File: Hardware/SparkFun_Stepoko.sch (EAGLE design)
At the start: 178 parts, among them J1 AVR ISP, Q1 16MHZ, Q2 100A/100V, U1 ATMEGA328, U10 +12v, U2 FT232RLSSOP, U3 74LVC1G04, U4 LM25011, U5 DRV8811, U6 74HC7014D, U7 7432SE, U8 DRV8811, U9 DRV8811

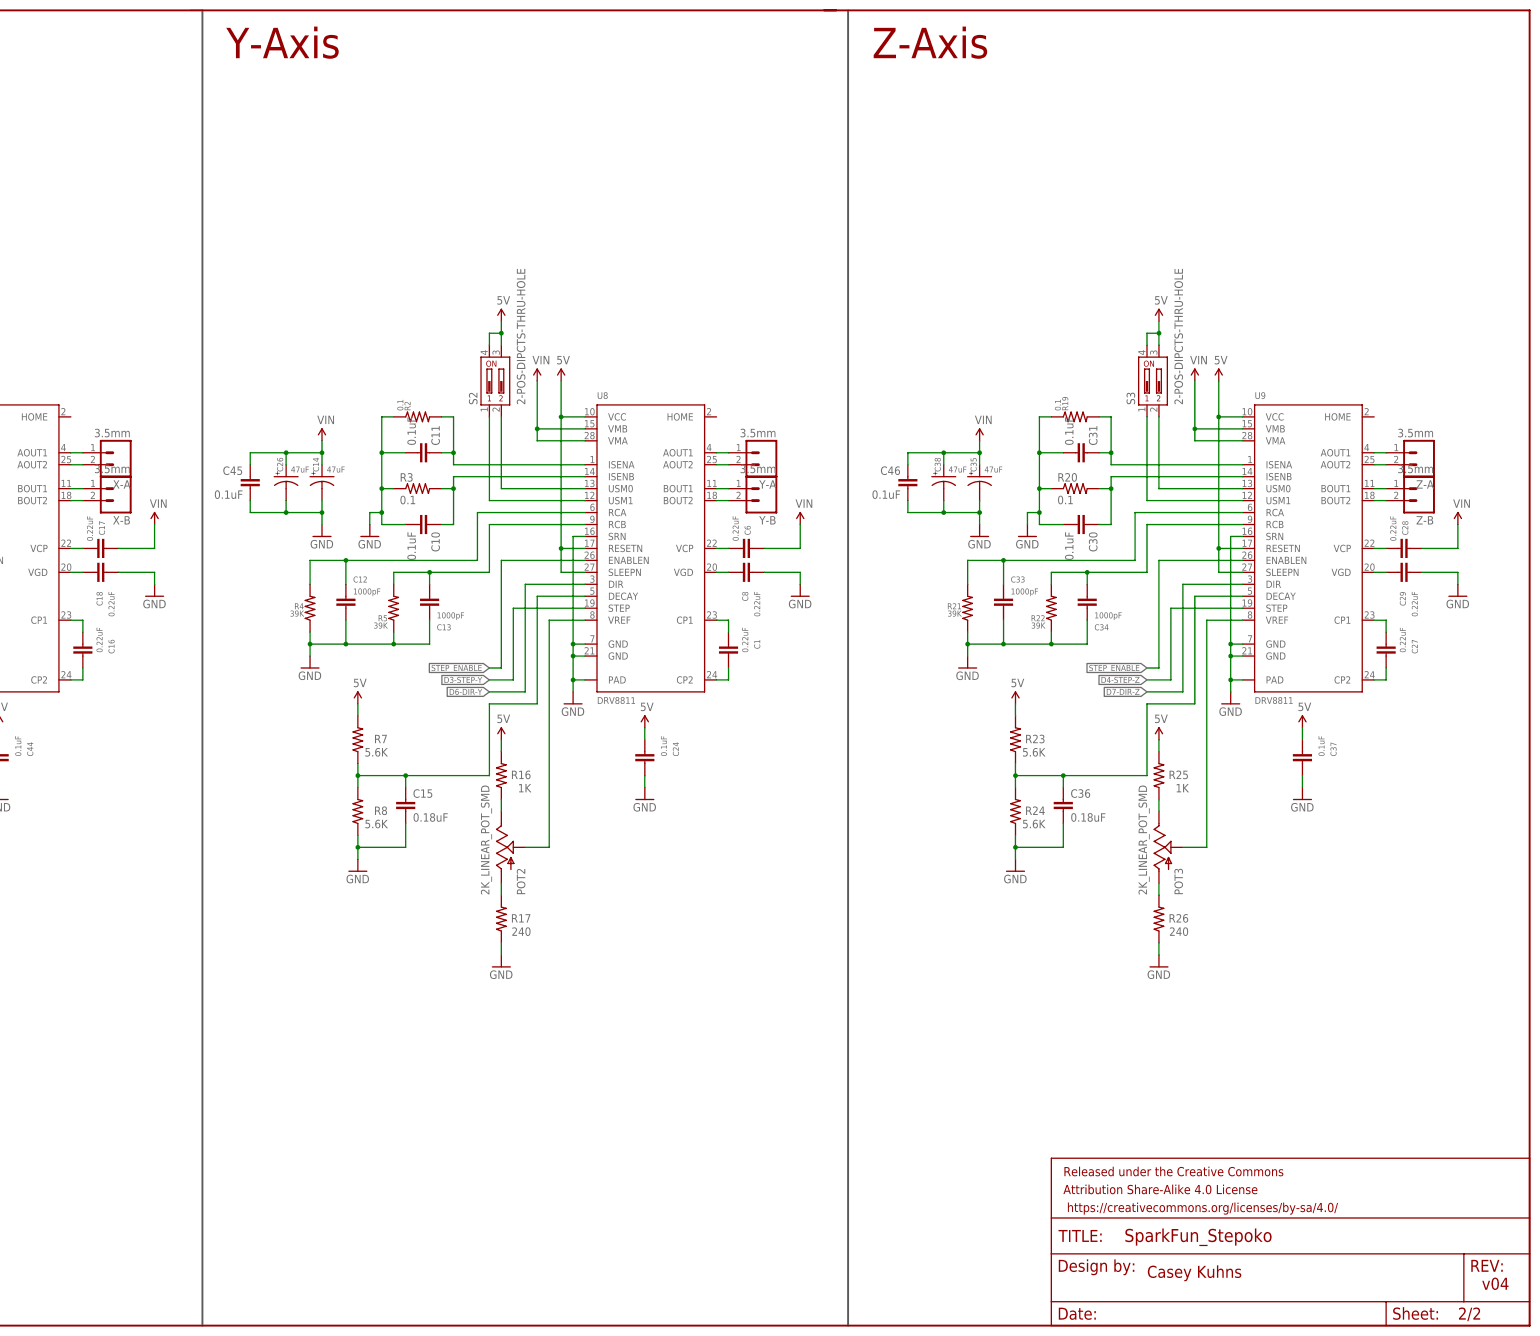
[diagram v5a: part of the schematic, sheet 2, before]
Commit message: corrected issued from Design review. Opened up holes to prevent potential shorts, schematic cleanup.
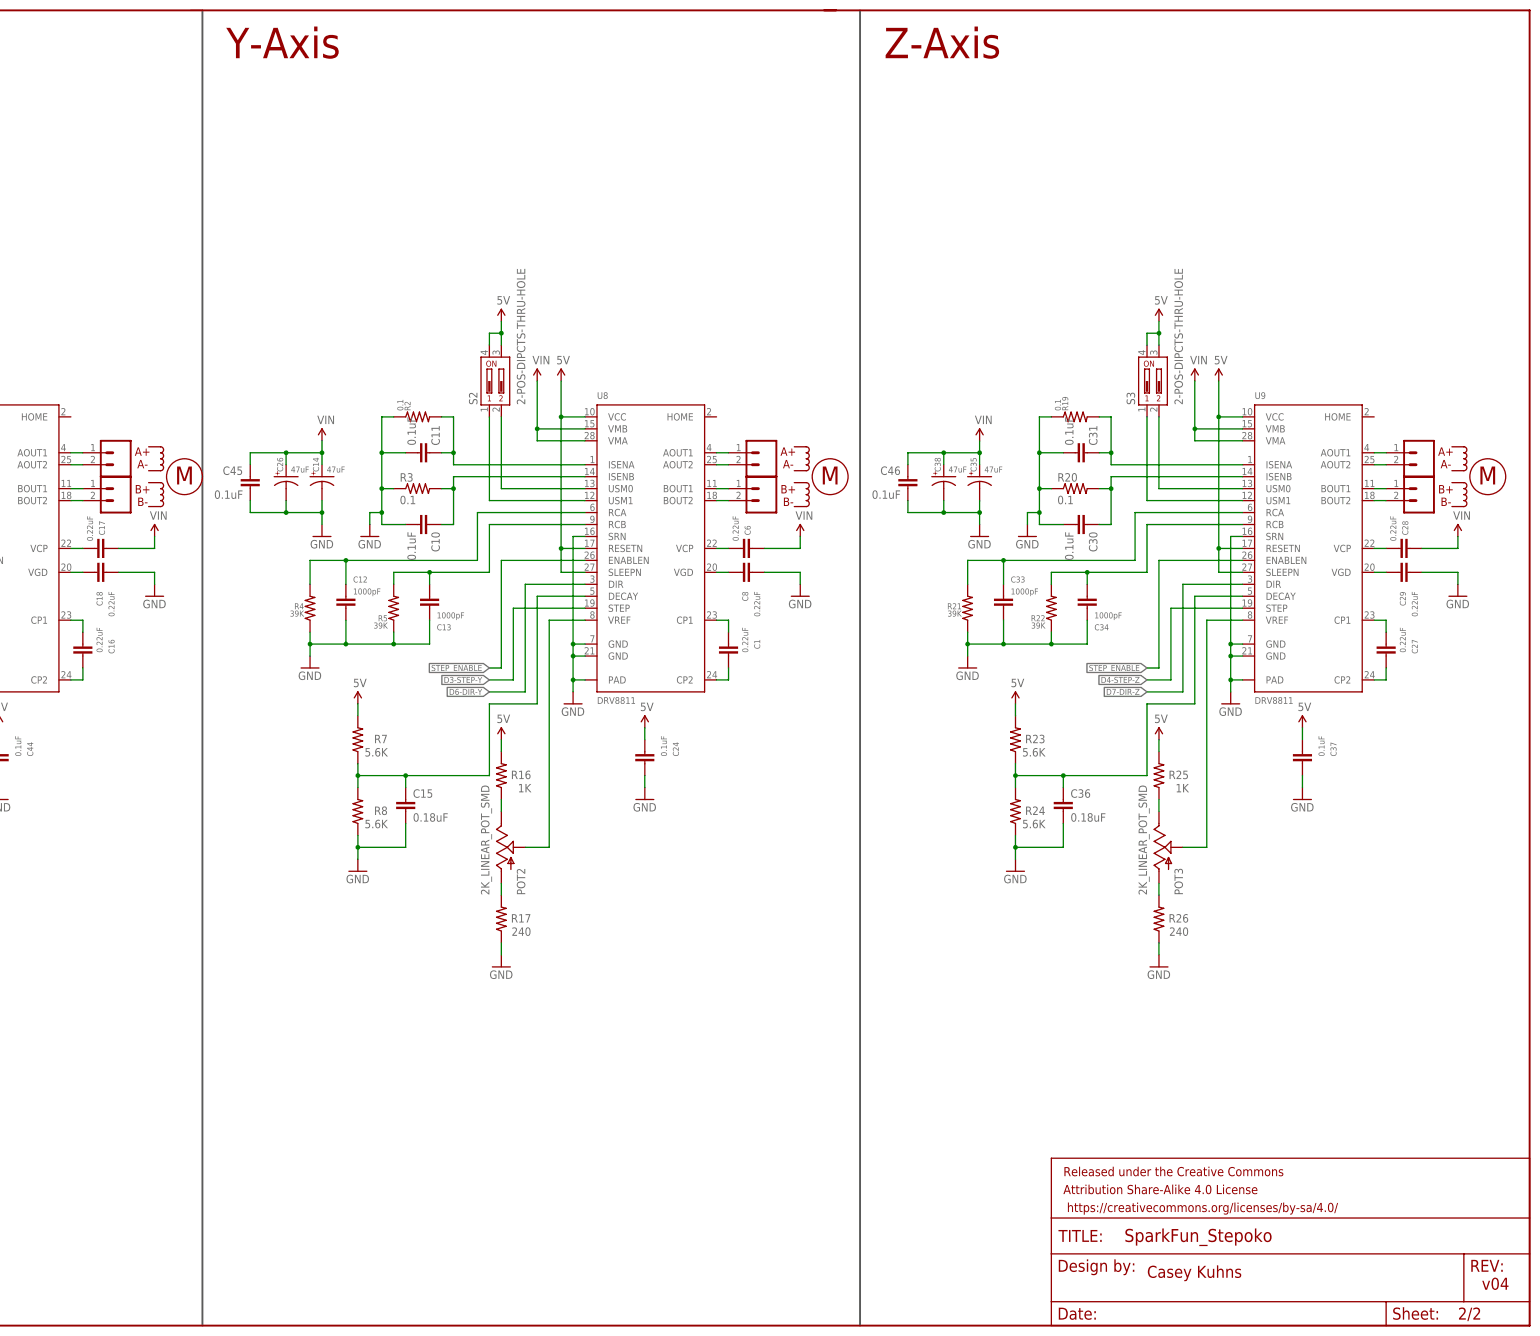
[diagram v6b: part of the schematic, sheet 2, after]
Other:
- note added: "A+ A- B+ B-"
- note added: "M"
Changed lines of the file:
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@@
 <setting verticaltext="up"/>
 </settings>
-<grid distance="0.1" unitdist="inch" unit="inch" style="lines" multiple="1" display="no" altdistance="0.01" altunitdist="inch" altunit="inch"/>
+<grid distance="0.1" unitdist="inch" unit="inch" style="lines" multiple="1" display="yes" altdistance="0.01" altunitdist="inch" altunit="inch"/>
 <layers>
 <layer number="1" name="Top" color="4" fill="1" visible="no" active="no"/>
@@
 <instance part="R52" gate="G$1" x="213.36" y="40.64" smashed="yes" rot="MR270">
 <attribute name="NAME" x="214.8586" y="36.83" size="1.778" layer="95" rot="MR90"/>
-<attribute name="VALUE" x="215.138" y="41.91" size="1.778" layer="96" rot="MR90"/>
+<attribute name="VALUE" x="210.058" y="36.83" size="1.778" layer="96" rot="MR90"/>
 </instance>
 <instance part="GND36" gate="1" x="213.36" y="30.48" rot="MR0"/>
@@
 <instance part="U10" gate="G$1" x="91.44" y="63.5" smashed="yes">
 <attribute name="NAME" x="86.36" y="55.88" size="1.778" layer="95"/>
-<attribute name="VALUE" x="86.36" y="73.66" size="1.778" layer="96"/>
+<attribute name="VALUE" x="86.36" y="53.34" size="1.778" layer="96"/>
 </instance>
 <instance part="GND60" gate="1" x="91.44" y="50.8" rot="MR0"/>
@@
 <text x="5.08" y="269.24" size="6.4516" layer="94" ratio="15">X-Axis</text>
 <text x="154.94" y="269.24" size="6.4516" layer="94" ratio="15">Y-Axis</text>
-<text x="292.1" y="269.24" size="6.4516" layer="94" ratio="15">Z-Axis</text>
+<text x="294.64" y="269.24" size="6.4516" layer="94" ratio="15">Z-Axis</text>
 <wire x1="147.32" y1="279.4" x2="149.86" y2="279.4" width="0.1524" layer="94"/>
 <wire x1="149.86" y1="279.4" x2="149.86" y2="0" width="0.4064" layer="97"/>
 <wire x1="284.48" y1="279.4" x2="281.94" y2="279.4" width="0.4064" layer="94"/>
-<wire x1="287.02" y1="279.4" x2="287.02" y2="0" width="0.4064" layer="97"/>
+<wire x1="289.56" y1="279.4" x2="289.56" y2="0" width="0.4064" layer="97"/>
 <text x="421.64" y="7.62" size="2.54" layer="94">v04</text>
 <text x="350.52" y="10.16" size="2.54" layer="94">Casey Kuhns</text>
+<wire x1="138.43" y1="181.61" x2="140.97" y2="181.61" width="0.1524" layer="94"/>
+<wire x1="138.43" y1="186.69" x2="140.97" y2="186.69" width="0.1524" layer="94"/>
+<wire x1="140.97" y1="186.69" x2="140.97" y2="185.42" width="0.1524" layer="94" curve="-180"/>
+<wire x1="140.97" y1="185.42" x2="140.97" y2="184.15" width="0.1524" layer="94" curve="-180"/>
+<wire x1="140.97" y1="184.15" x2="140.97" y2="182.88" width="0.1524" layer="94" curve="-180"/>
+<wire x1="140.97" y1="182.88" x2="140.97" y2="181.61" width="0.1524" layer="94" curve="-180"/>
+<wire x1="138.43" y1="173.99" x2="140.97" y2="173.99" width="0.1524" layer="94"/>
+<wire x1="138.43" y1="179.07" x2="140.97" y2="179.07" width="0.1524" layer="94"/>
+<wire x1="140.97" y1="179.07" x2="140.97" y2="177.8" width="0.1524" layer="94" curve="-180"/>
+<wire x1="140.97" y1="177.8" x2="140.97" y2="176.53" width="0.1524" layer="94" curve="-180"/>
+<wire x1="140.97" y1="176.53" x2="140.97" y2="175.26" width="0.1524" layer="94" curve="-180"/>
+<wire x1="140.97" y1="175.26" x2="140.97" y2="173.99" width="0.1524" layer="94" curve="-180"/>
+<circle x="146.05" y="180.34" radius="3.81" width="0.1524" layer="94"/>
+<text x="146.05" y="180.594" size="3.81" layer="94" font="fixed" ratio="14" align="center">M</text>
+<wire x1="275.59" y1="181.61" x2="278.13" y2="181.61" width="0.1524" layer="94"/>
+<wire x1="275.59" y1="186.69" x2="278.13" y2="186.69" width="0.1524" layer="94"/>
+<wire x1="278.13" y1="186.69" x2="278.13" y2="185.42" width="0.1524" layer="94" curve="-180"/>
+<wire x1="278.13" y1="185.42" x2="278.13" y2="184.15" width="0.1524" layer="94" curve="-180"/>
+<wire x1="278.13" y1="184.15" x2="278.13" y2="182.88" width="0.1524" layer="94" curve="-180"/>
+<wire x1="278.13" y1="182.88" x2="278.13" y2="181.61" width="0.1524" layer="94" curve="-180"/>
+<wire x1="275.59" y1="173.99" x2="278.13" y2="173.99" width="0.1524" layer="94"/>
+<wire x1="275.59" y1="179.07" x2="278.13" y2="179.07" width="0.1524" layer="94"/>
+<wire x1="278.13" y1="179.07" x2="278.13" y2="177.8" width="0.1524" layer="94" curve="-180"/>
+<wire x1="278.13" y1="177.8" x2="278.13" y2="176.53" width="0.1524" layer="94" curve="-180"/>
+<wire x1="278.13" y1="176.53" x2="278.13" y2="175.26" width="0.1524" layer="94" curve="-180"/>
+<wire x1="278.13" y1="175.26" x2="278.13" y2="173.99" width="0.1524" layer="94" curve="-180"/>
+<circle x="283.21" y="180.34" radius="3.81" width="0.1524" layer="94"/>
+<text x="283.21" y="180.594" size="3.81" layer="94" font="fixed" ratio="14" align="center">M</text>
+<wire x1="415.29" y1="181.61" x2="417.83" y2="181.61" width="0.1524" layer="94"/>
+<wire x1="415.29" y1="186.69" x2="417.83" y2="186.69" width="0.1524" layer="94"/>
+<wire x1="417.83" y1="186.69" x2="417.83" y2="185.42" width="0.1524" layer="94" curve="-180"/>
+<wire x1="417.83" y1="185.42" x2="417.83" y2="184.15" width="0.1524" layer="94" curve="-180"/>
+<wire x1="417.83" y1="184.15" x2="417.83" y2="182.88" width="0.1524" layer="94" curve="-180"/>
+<wire x1="417.83" y1="182.88" x2="417.83" y2="181.61" width="0.1524" layer="94" curve="-180"/>
+<wire x1="415.29" y1="173.99" x2="417.83" y2="173.99" width="0.1524" layer="94"/>
+<wire x1="415.29" y1="179.07" x2="417.83" y2="179.07" width="0.1524" layer="94"/>
+<wire x1="417.83" y1="179.07" x2="417.83" y2="177.8" width="0.1524" layer="94" curve="-180"/>
+<wire x1="417.83" y1="177.8" x2="417.83" y2="176.53" width="0.1524" layer="94" curve="-180"/>
+<wire x1="417.83" y1="176.53" x2="417.83" y2="175.26" width="0.1524" layer="94" curve="-180"/>
+<wire x1="417.83" y1="175.26" x2="417.83" y2="173.99" width="0.1524" layer="94" curve="-180"/>
+<circle x="422.91" y="180.34" radius="3.81" width="0.1524" layer="94"/>
+<text x="422.91" y="180.594" size="3.81" layer="94" font="fixed" ratio="14" align="center">M</text>
+<text x="137.16" y="180.34" size="1.778" layer="94" ratio="14" align="center">A+
+A-
+B+
+B-</text>
+<text x="274.32" y="180.34" size="1.778" layer="94" ratio="14" align="center">A+
+A-
+B+
+B-</text>
+<text x="414.02" y="180.34" size="1.778" layer="94" ratio="14" align="center">A+
+A-
+B+
+B-</text>
 </plain>
 <instances>
@@
 <instance part="GND29" gate="1" x="106.68" y="111.76"/>
 <instance part="SUPPLY3" gate="G$1" x="83.82" y="200.66"/>
-<instance part="SUPPLY5" gate="G$1" x="139.7" y="170.18"/>
+<instance part="SUPPLY5" gate="G$1" x="139.7" y="167.64"/>
 <instance part="POT1" gate="G$1" x="76.2" y="101.6"/>
 <instance part="R1" gate="G$1" x="76.2" y="86.36" smashed="yes" rot="R90">
@@
 <attribute name="VALUE" x="82.55" y="84.582" size="1.778" layer="96" rot="R180"/>
 </instance>
-<instance part="X-A" gate="G$1" x="132.08" y="185.42" rot="R180"/>
-<instance part="X-B" gate="G$1" x="132.08" y="177.8" rot="R180"/>
+<instance part="X-A" gate="G$1" x="132.08" y="185.42" smashed="yes" rot="R180"/>
+<instance part="X-B" gate="G$1" x="132.08" y="177.8" smashed="yes" rot="R180"/>
 <instance part="FRAME2" gate="G$1" x="0" y="0"/>
 <instance part="FRAME2" gate="G$2" x="330.2" y="0"/>
@@
 <instance part="GND19" gate="1" x="243.84" y="111.76"/>
 <instance part="SUPPLY6" gate="G$1" x="220.98" y="200.66"/>
-<instance part="SUPPLY7" gate="G$1" x="276.86" y="170.18"/>
+<instance part="SUPPLY7" gate="G$1" x="276.86" y="167.64"/>
 <instance part="POT2" gate="G$1" x="213.36" y="101.6"/>
 <instance part="R17" gate="G$1" x="213.36" y="86.36" smashed="yes" rot="R90">
@@
 <attribute name="VALUE" x="219.71" y="84.582" size="1.778" layer="96" rot="R180"/>
 </instance>
-<instance part="Y-A" gate="G$1" x="269.24" y="185.42" rot="R180"/>
-<instance part="Y-B" gate="G$1" x="269.24" y="177.8" rot="R180"/>
+<instance part="Y-A" gate="G$1" x="269.24" y="185.42" smashed="yes" rot="R180"/>
+<instance part="Y-B" gate="G$1" x="269.24" y="177.8" smashed="yes" rot="R180"/>
 <instance part="U8" gate="G$1" x="246.38" y="167.64"/>
 <instance part="S2" gate="G$1" x="210.82" y="200.66"/>
@@
 <instance part="GND54" gate="1" x="383.54" y="111.76"/>
 <instance part="SUPPLY35" gate="G$1" x="360.68" y="200.66"/>
-<instance part="SUPPLY36" gate="G$1" x="416.56" y="170.18"/>
+<instance part="SUPPLY36" gate="G$1" x="416.56" y="167.64"/>
 <instance part="POT3" gate="G$1" x="353.06" y="101.6"/>
 <instance part="R26" gate="G$1" x="353.06" y="86.36" smashed="yes" rot="R90">
@@
 <attribute name="VALUE" x="359.41" y="84.582" size="1.778" layer="96" rot="R180"/>
 </instance>
-<instance part="Z-A" gate="G$1" x="408.94" y="185.42" rot="R180"/>
-<instance part="Z-B" gate="G$1" x="408.94" y="177.8" rot="R180"/>
+<instance part="Z-A" gate="G$1" x="408.94" y="185.42" smashed="yes" rot="R180"/>
+<instance part="Z-B" gate="G$1" x="408.94" y="177.8" smashed="yes" rot="R180"/>
 <instance part="U9" gate="G$1" x="386.08" y="167.64"/>
 <instance part="S3" gate="G$1" x="350.52" y="200.66"/>
@@
 <pinref part="C17" gate="G$1" pin="1"/>
 <pinref part="SUPPLY5" gate="G$1" pin="VIN"/>
-<wire x1="139.7" y1="170.18" x2="139.7" y2="165.1" width="0.1524" layer="91"/>
+<wire x1="139.7" y1="167.64" x2="139.7" y2="165.1" width="0.1524" layer="91"/>
 <wire x1="139.7" y1="165.1" x2="132.08" y2="165.1" width="0.1524" layer="91"/>
 </segment>
@@
 <pinref part="C6" gate="G$1" pin="1"/>
 <pinref part="SUPPLY7" gate="G$1" pin="VIN"/>
-<wire x1="276.86" y1="170.18" x2="276.86" y2="165.1" width="0.1524" layer="91"/>
+<wire x1="276.86" y1="167.64" x2="276.86" y2="165.1" width="0.1524" layer="91"/>
 <wire x1="276.86" y1="165.1" x2="269.24" y2="165.1" width="0.1524" layer="91"/>
 </segment>
@@
 <pinref part="C28" gate="G$1" pin="1"/>
 <pinref part="SUPPLY36" gate="G$1" pin="VIN"/>
-<wire x1="416.56" y1="170.18" x2="416.56" y2="165.1" width="0.1524" layer="91"/>
+<wire x1="416.56" y1="167.64" x2="416.56" y2="165.1" width="0.1524" layer="91"/>
 <wire x1="416.56" y1="165.1" x2="408.94" y2="165.1" width="0.1524" layer="91"/>
 </segment>

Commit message: updated version number
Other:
- note added: "v10"
- note removed: "v04"
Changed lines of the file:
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@@
 <setting verticaltext="up"/>
 </settings>
-<grid distance="0.1" unitdist="inch" unit="inch" style="lines" multiple="1" display="yes" altdistance="0.01" altunitdist="inch" altunit="inch"/>
+<grid distance="0.1" unitdist="inch" unit="inch" style="lines" multiple="1" display="no" altdistance="0.01" altunitdist="inch" altunit="inch"/>
 <layers>
 <layer number="1" name="Top" color="4" fill="1" visible="no" active="no"/>
@@
 <text x="81.28" y="38.1" size="1.778" layer="97" rot="R90">Power</text>
 <text x="350.52" y="10.16" size="2.54" layer="94">Casey Kuhns</text>
-<text x="421.64" y="7.62" size="2.54" layer="94">v04</text>
+<text x="421.64" y="7.62" size="2.54" layer="94">v10</text>
 <text x="132.08" y="99.06" size="1.778" layer="97">D0- RX
 D1- TX
@@
 <wire x1="284.48" y1="279.4" x2="281.94" y2="279.4" width="0.4064" layer="94"/>
 <wire x1="289.56" y1="279.4" x2="289.56" y2="0" width="0.4064" layer="97"/>
-<text x="421.64" y="7.62" size="2.54" layer="94">v04</text>
+<text x="421.64" y="7.62" size="2.54" layer="94">v10</text>
 <text x="350.52" y="10.16" size="2.54" layer="94">Casey Kuhns</text>
 <wire x1="138.43" y1="181.61" x2="140.97" y2="181.61" width="0.1524" layer="94"/>
